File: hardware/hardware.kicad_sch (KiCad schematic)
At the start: 0 parts

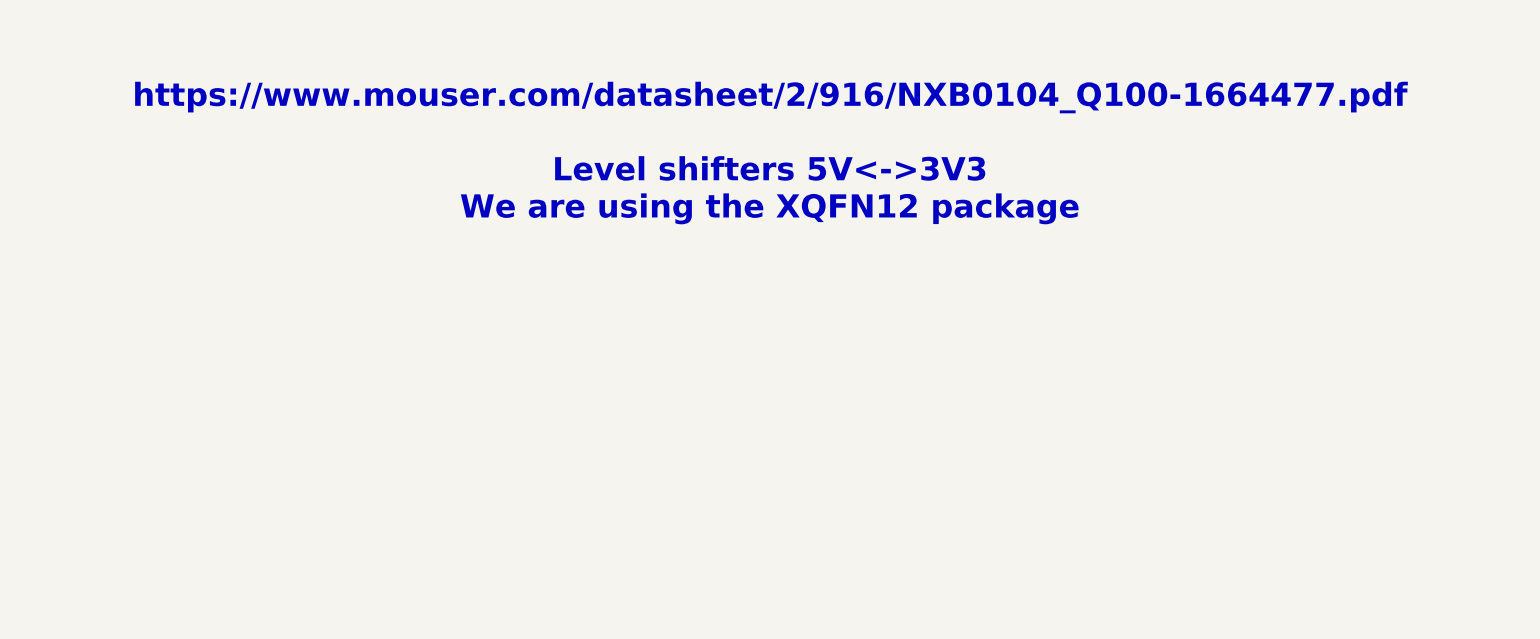
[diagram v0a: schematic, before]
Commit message: add hardware stuff for symbol/footprint of level shifter
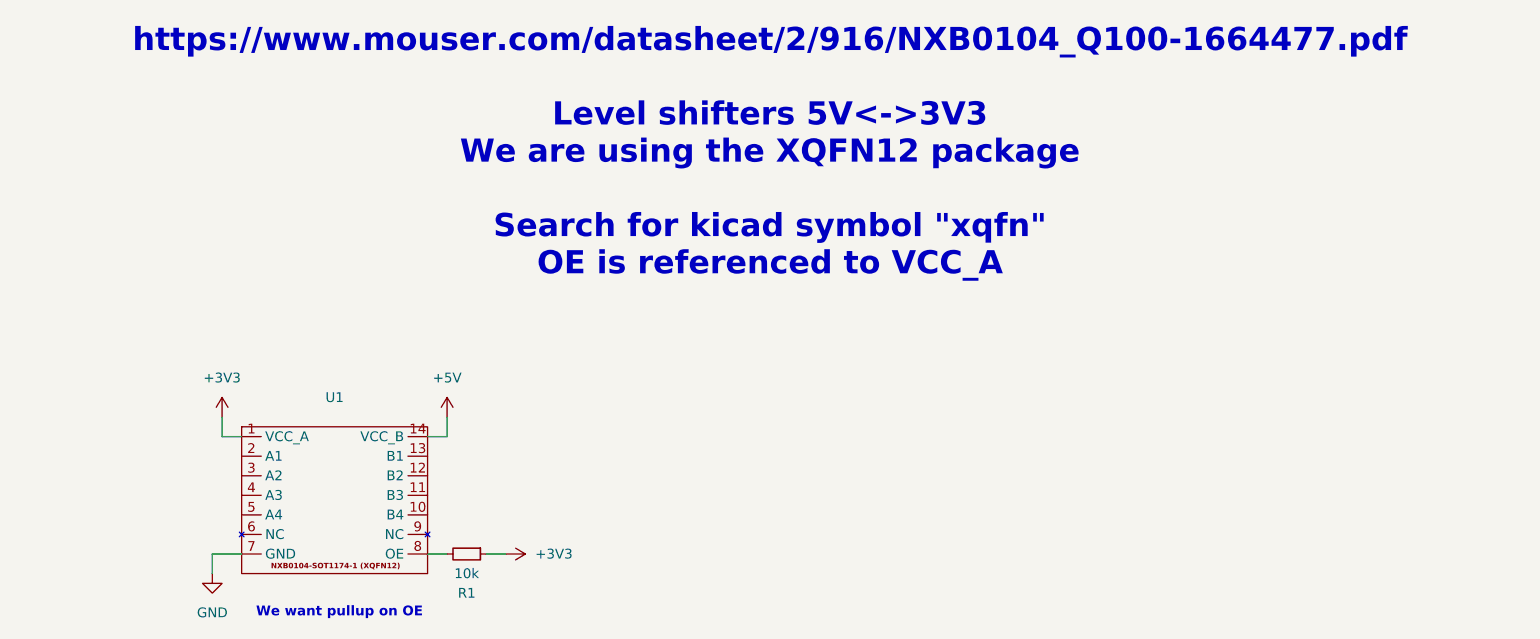
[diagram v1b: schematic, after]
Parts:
- added R1: 10k, symbol Device:R_Small
- added U1: ~, symbol custom_symbols:NXB0104_XQFN12
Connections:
- new net: R1.2, U1.8 (OE)
- new net +3V3: R1.1, U1.1 (VCC_A)
- new net +5V: U1.14 (VCC_B)
- new net GND: U1.7 (GND)
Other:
- note added: "We want pullup on OE"
- note added: "https://www.mouser.com/datasheet/2/916/NXB0104_Q100-1664477.pdf Level shifters 5V<->3V3 We are using the XQFN12 package Search for kicad symbol "xqfn" OE is referenced to VCC_A"
- note removed: "https://www.mouser.com/datasheet/2/916/NXB0104_Q100-1664477.pdf Level shifters 5V<->3V3 We are using the XQFN12 package"
